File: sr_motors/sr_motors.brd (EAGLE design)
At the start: 78.4 x 64.8 mm, 20 parts

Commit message: Added reverse current protection for external power, added version text
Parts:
- added Q1: IRLML2244TRPbF, we-transistor:SOT23
- moved C2 4.02 mm to (20.3, 5.08), turned to 0 degrees
- turned EXT_PWR_IN to 180 degrees
- turned EXT_PWR_OUT to 180 degrees
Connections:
- new net VCC2_RAW: EXT_PWR_IN.1, Q1.3
- net GND: now also Q1.1
- net VCC2: now also Q1.2; no longer EXT_PWR_IN.1
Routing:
- net GND: track 287.8 -> 364.7 mm
- net VCC2: track 99.2 -> 91.9 mm
- net VCC2_RAW: track 0.00 -> 2.71 mm
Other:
- board text added: "sr_motors v1.1 git.io/v6yCJ"

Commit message: Increased width of power lines on sr_motors
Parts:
- moved C2 2.54 mm to (20.3, 7.62), turned to 270 degrees
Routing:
- net GND: track 364.7 -> 345.6 mm
- net VCC2: track 91.9 -> 84.6 mm
- net VCC1: track 227.6 -> 223.8 mm

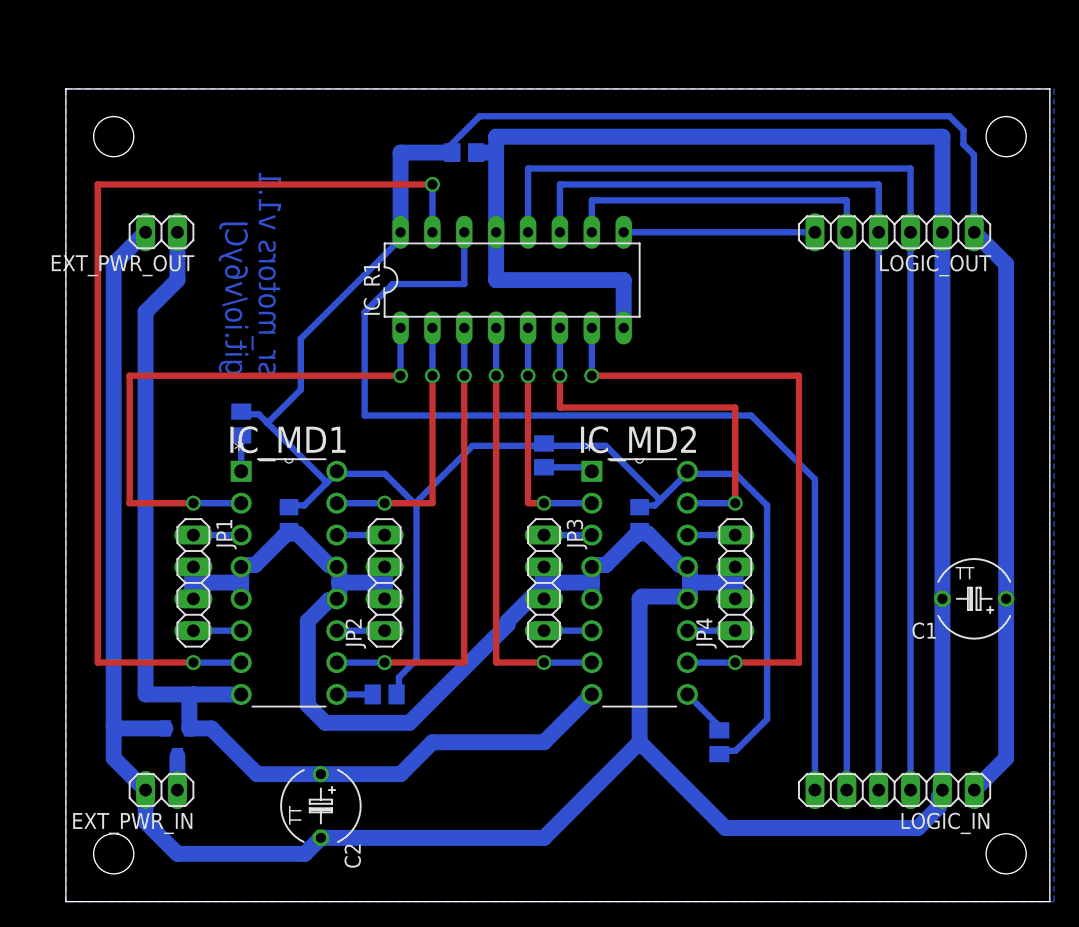
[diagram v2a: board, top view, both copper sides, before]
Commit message: Icreased width of routes, icreased board width
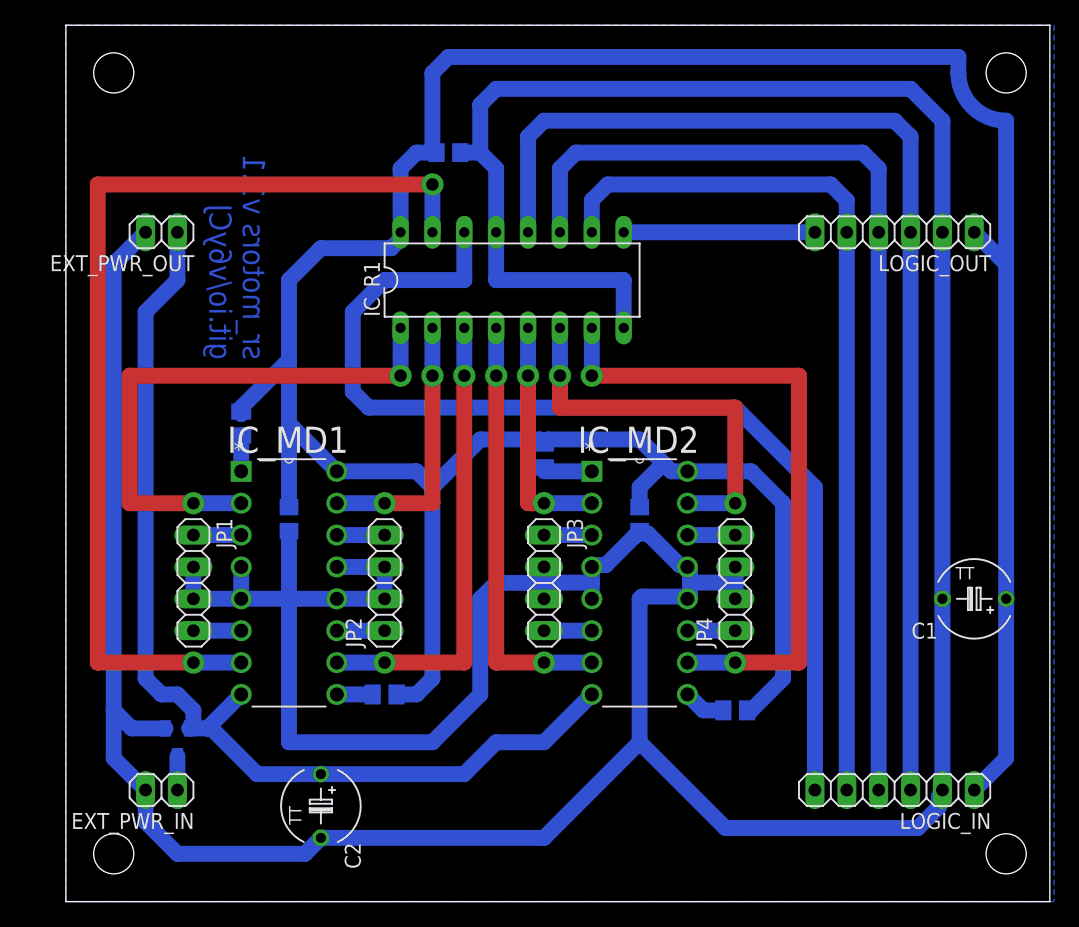
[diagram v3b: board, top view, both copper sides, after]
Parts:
- moved R14 2.84 mm to (53.3, 15.2), turned to 180 degrees
- moved C3 1.27 mm to (30.5, 59.7)
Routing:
- net VCC1: track 223.8 -> 244.0 mm
- net GND: track 345.6 -> 365.2 mm
- net RCK: track 85.1 -> 91.2 mm
- net SCK: track 77.5 -> 81.1 mm
- net VCC2: track 84.6 -> 83.3 mm
- net SCLR: track 69.8 -> 70.9 mm
- net EN3: track 3.91 -> 3.39 mm
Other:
- board size 78.4 x 64.8 mm -> 78.4 x 69.8 mm
